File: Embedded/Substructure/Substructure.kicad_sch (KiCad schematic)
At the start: 12 parts, among them J1 Power, U1 Expansion, U2 TCA9535RTWR, U3 TOF 0, U4 TOF 1, U5 OLED, U6 FFC [D]

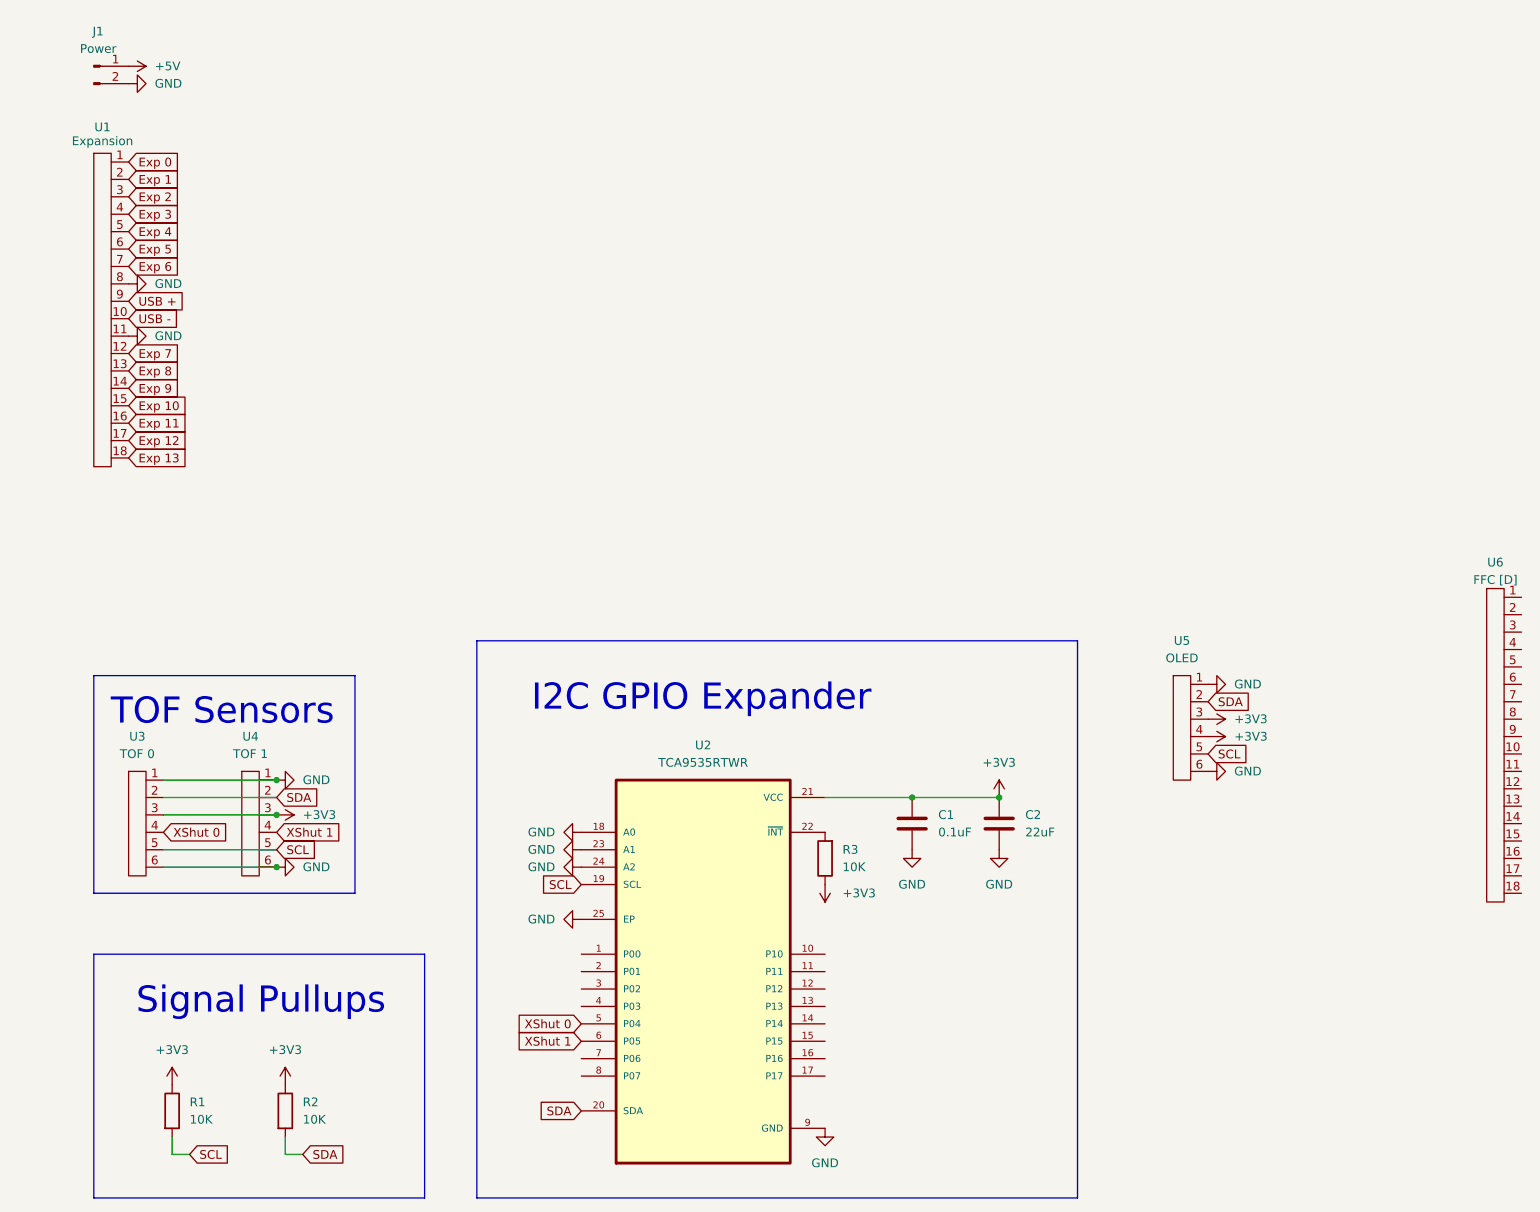
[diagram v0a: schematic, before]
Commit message: Added USB-2WComms Solder Bridge
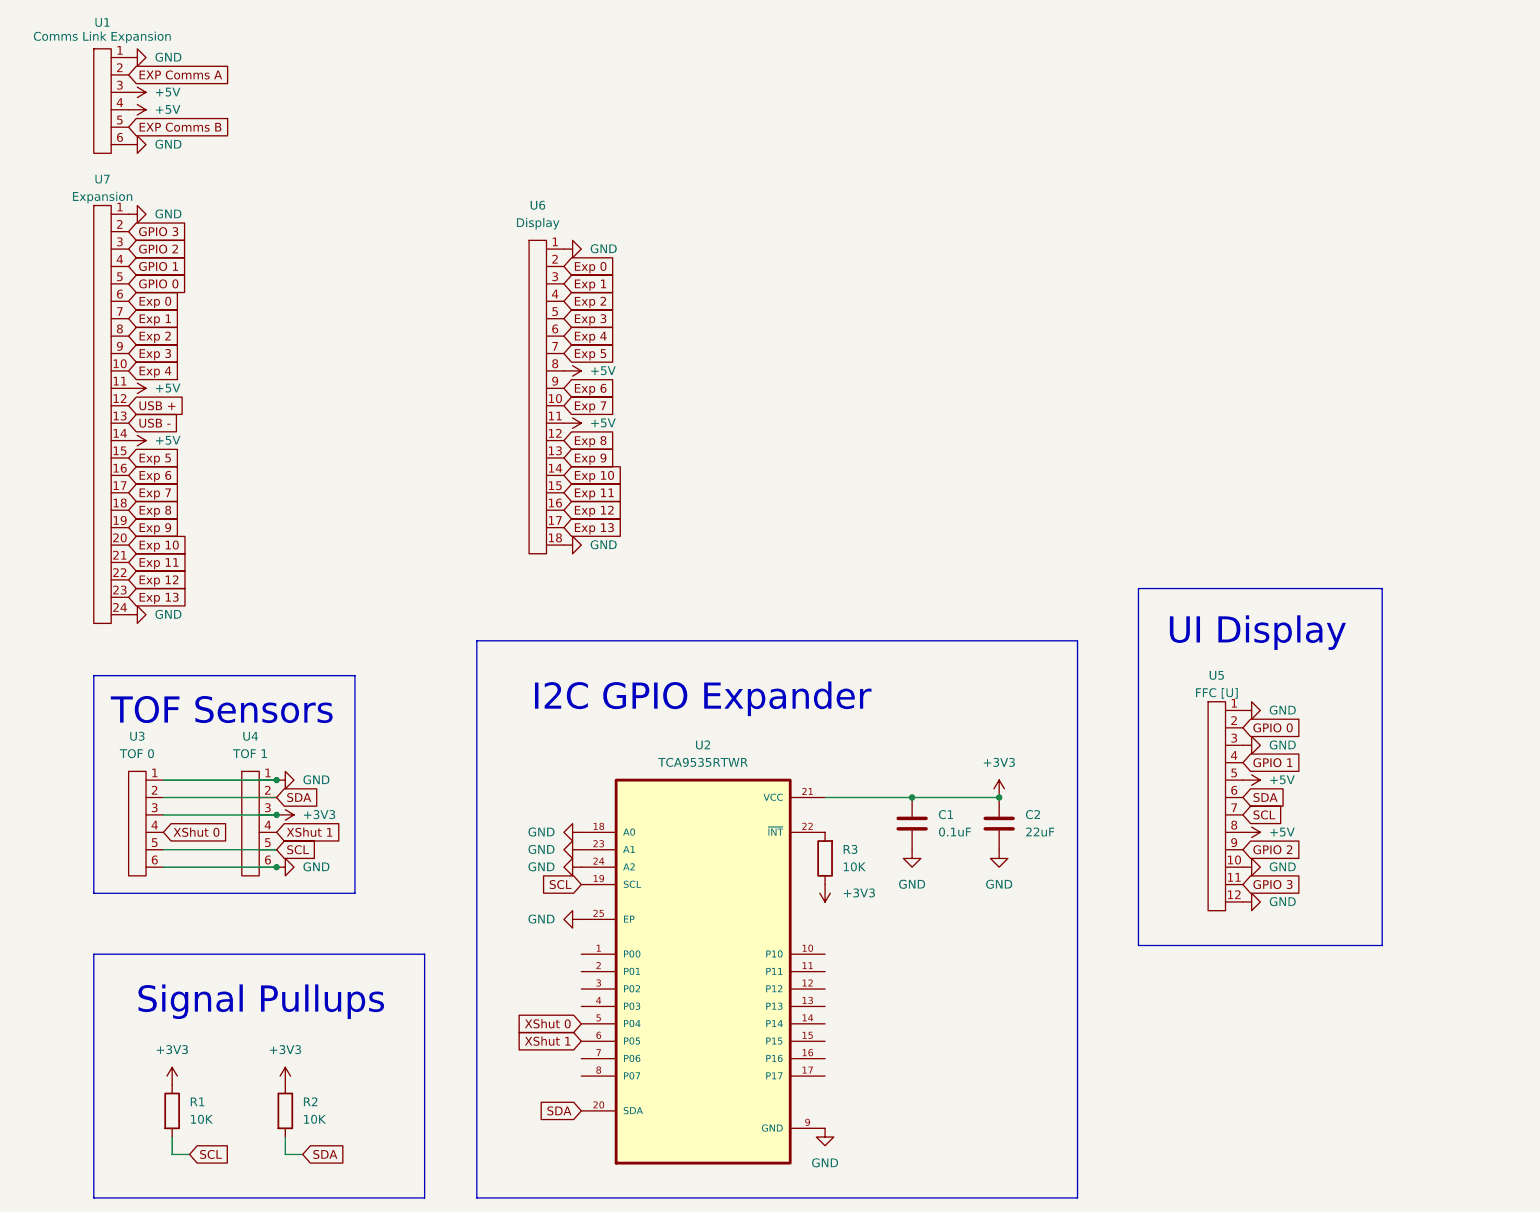
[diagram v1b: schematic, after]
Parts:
- removed J1: Power, Connector_Hirose:Hirose_DF13-02P-1.25DS_1x02_P1.25mm_Horizontal, symbol Connector:Conn_01x02_Pin
- removed U1: Expansion, FFC_Connector:FFC Aliexpress 0.5mm 18P, symbol FCC_Connector:FFC_18P
- removed U5: OLED, FFC_Connector:FFC Aliexpress 0.5mm 6P, symbol FCC_Connector:FFC_6P
- added U1: Comms Link Expansion, FFC_Connector:FFC Aliexpress 0.5mm 6P, symbol FCC_Connector:FFC_6P
- added U5: FFC [U], FFC_Connector:FFC Aliexpress 0.5mm 12P, symbol FCC_Connector:FFC_12P
- added U7: Expansion, FFC_Connector:FFC Aliexpress 0.5mm 24P, symbol FCC_Connector:FFC_24P
- U3, U4: footprint FFC_Connector:FFC Aliexpress 0.5mm 6P -> Connector_Hirose:Hirose_DF13-06P-1.25DS_1x06_P1.25mm_Horizontal
- U6: value FFC [D] -> Display
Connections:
- net +5V: now also U6.11, U6.8, U1.3, U1.4, U5.5, U5.8, U7.11, U7.14
- net Exp 0: now also U6.2, U7.6
- net Exp 1: now also U6.3, U7.7
- net Exp 10: now also U6.14, U7.20
- net Exp 11: now also U6.15, U7.21
- net Exp 12: now also U6.16, U7.22
- net Exp 13: now also U6.17, U7.23
- net Exp 2: now also U6.4, U7.8
- net Exp 3: now also U6.5, U7.9
- net Exp 4: now also U6.6, U7.10
- net Exp 5: now also U6.7, U7.15
- net Exp 6: now also U6.9, U7.16
- net Exp 7: now also U6.10, U7.17
- net Exp 8: now also U6.12, U7.18
- net Exp 9: now also U6.13, U7.19
- net GND: now also U6.1, U6.18, U1.1, U1.6, U5.1, U5.10, U5.12, U5.3, U7.1, U7.24
- net SCL: now also U5.7
- net SDA: now also U5.6
- net USB +: now also U7.12
- net USB -: now also U7.13
- new net EXP Comms A: U1.2
- new net EXP Comms B: U1.5
- new net GPIO 0: U5.2, U7.5
- new net GPIO 1: U5.4, U7.4
- new net GPIO 2: U5.9, U7.3
- new net GPIO 3: U5.11, U7.2
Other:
- note added: "UI Display"
- moved on the sheet: U6
